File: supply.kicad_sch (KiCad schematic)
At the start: 66 parts, among them U5 PAC1934_QFN

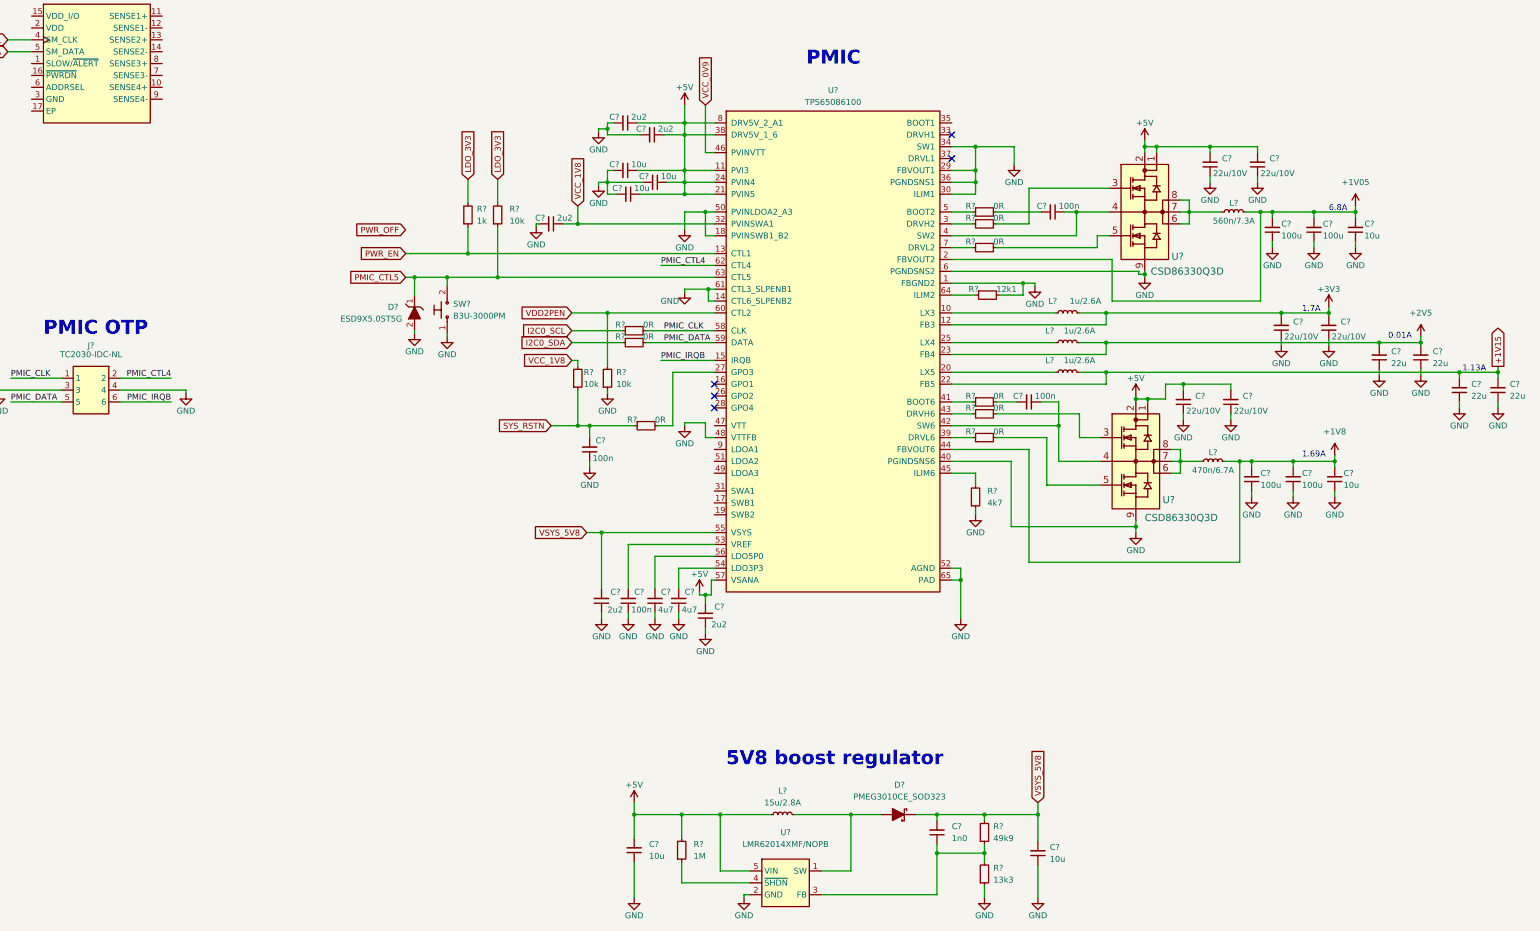
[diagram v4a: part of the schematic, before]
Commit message: [#52577] Change PMIC's inductors
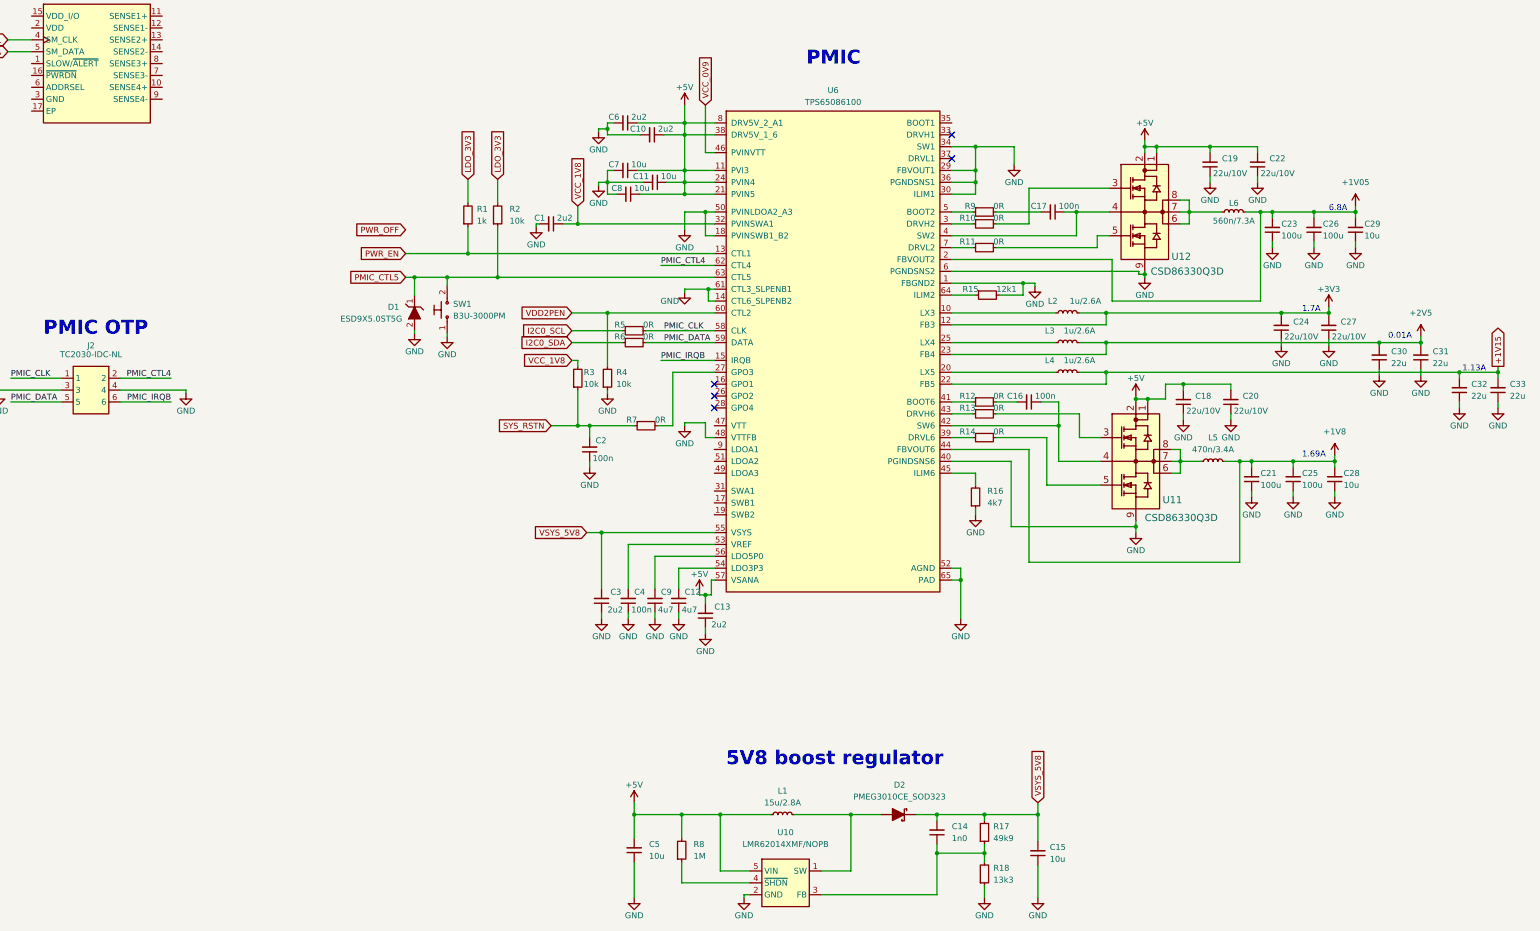
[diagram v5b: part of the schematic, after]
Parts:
- removed L?: L_470n_6.7A_Vishay-IHLP-1212AE-11, antmicro-footprints:L_Vishay-IHLP-1212AE, symbol antmicroFixedInductors:L_470n_6.7A_Vishay-IHLP-1212AE-11
- added L5: L_470n_3.4A_WE-MAIA-2512, antmicro-footprints:L_WE-MAIA-2512, symbol antmicroFixedInductors:L_470n_3.4A_WE-MAIA-2512
- gave numbers to parts that had none: 64
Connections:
- net +1V8: now also L5.2
- net at U11.6 (VSW), U11.7 (VSW), U11.8 (VSW): now also L5.1

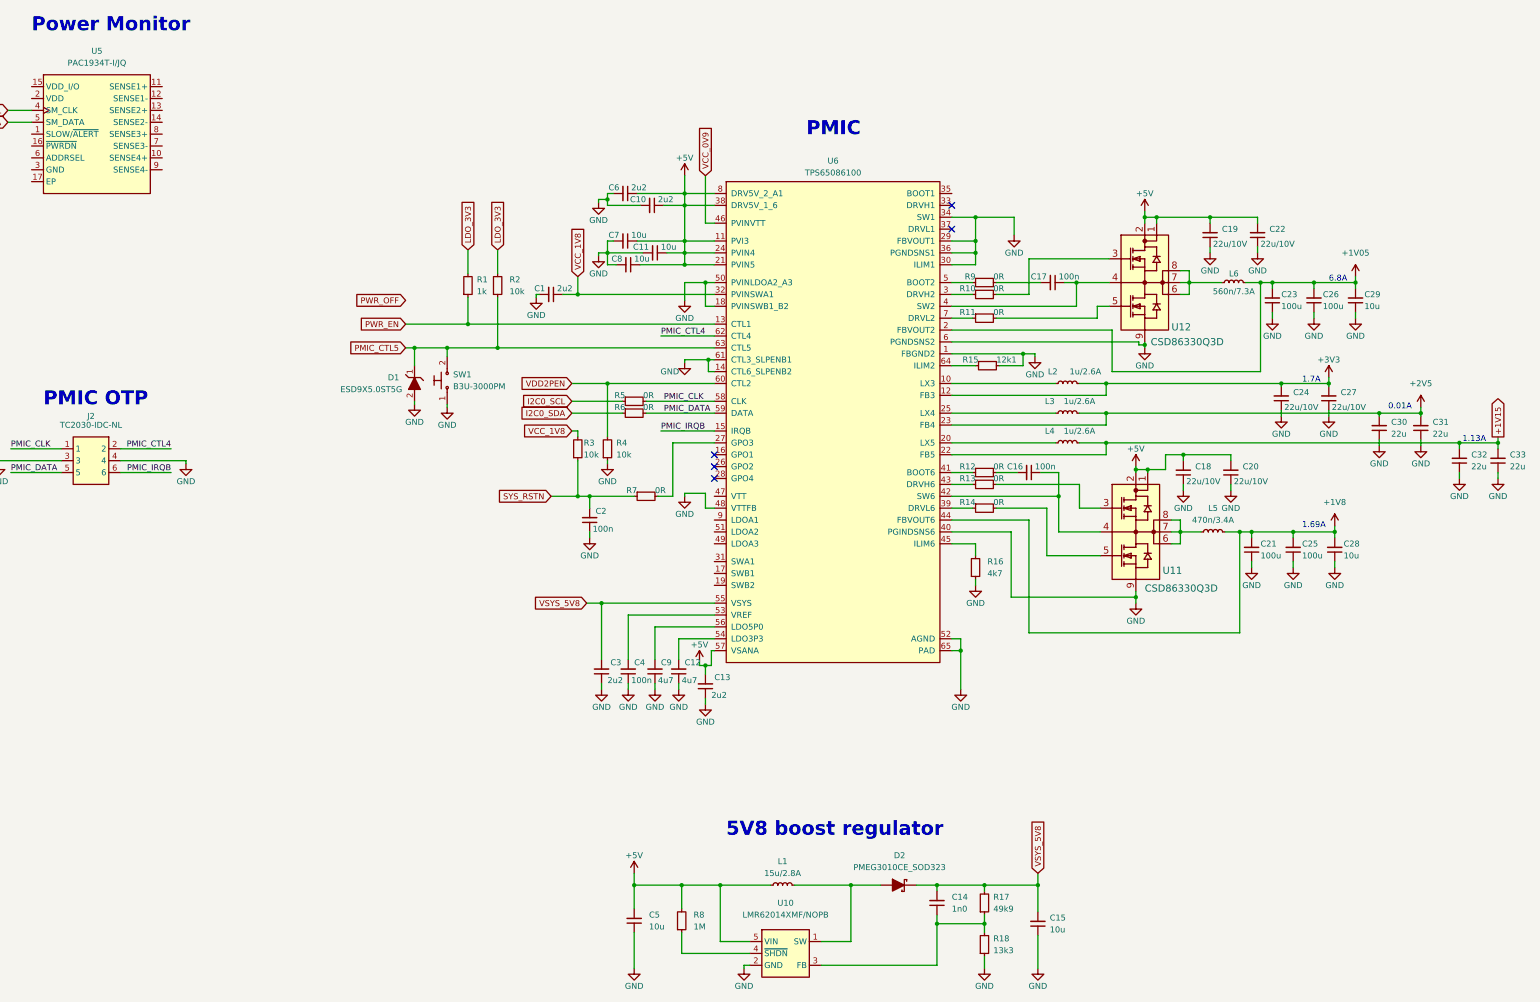
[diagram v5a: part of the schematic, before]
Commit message: [#52577] Clear annotations
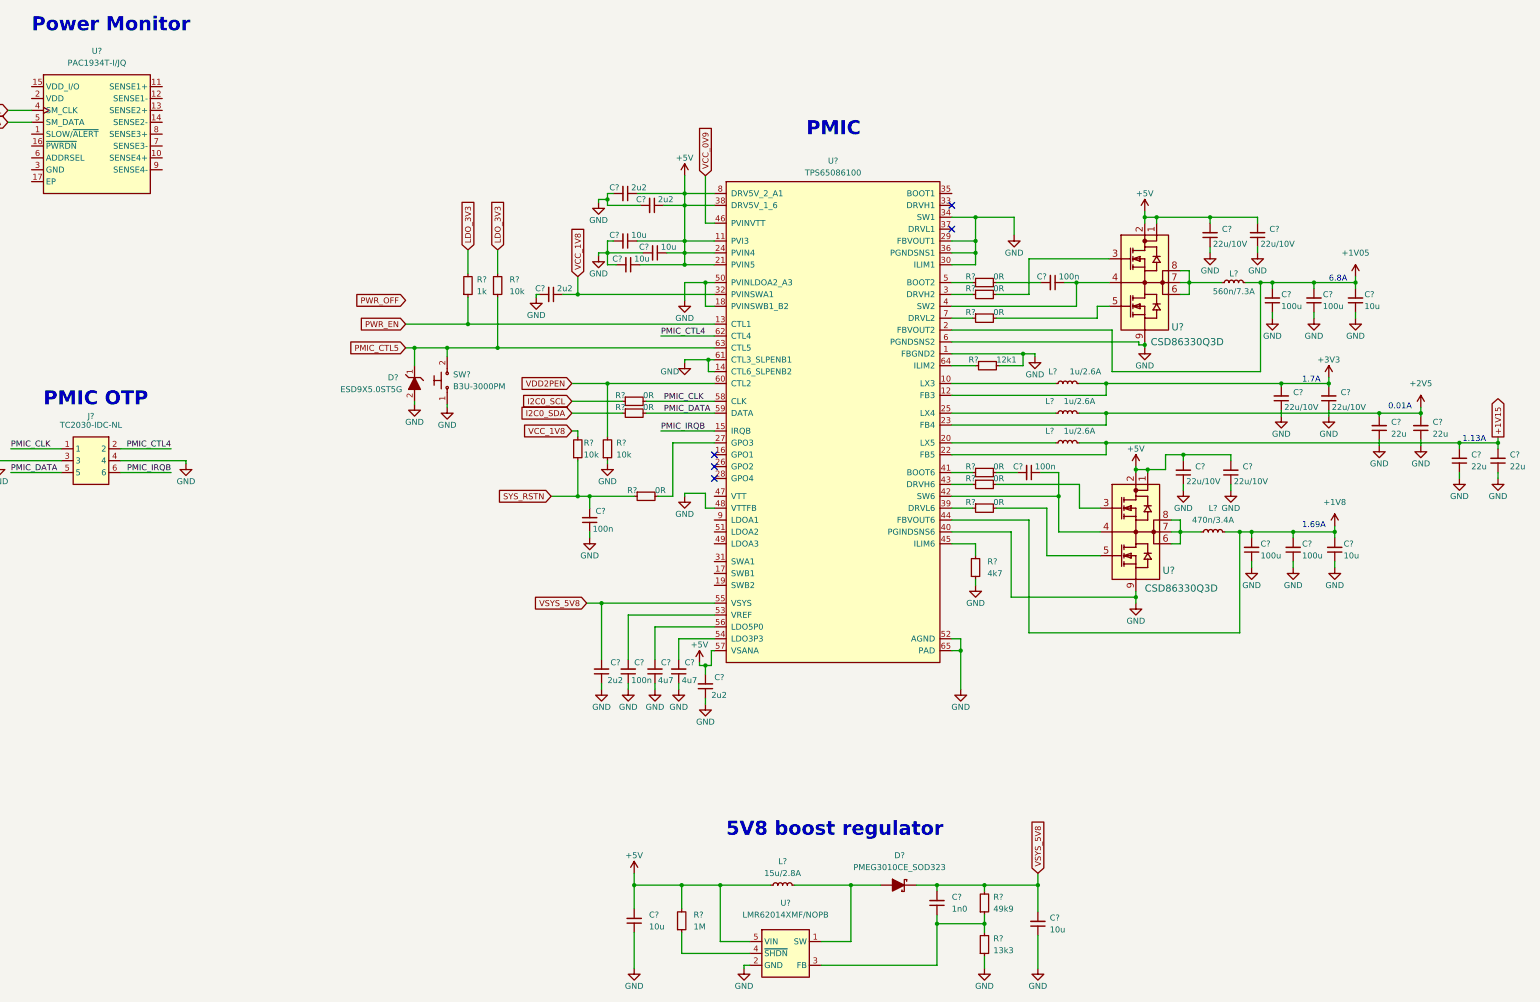
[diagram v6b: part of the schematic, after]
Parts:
- renumbered C14 to C?, C28 to C?, C31 to C?, C8 to C?, C29 to C?, C15 to C?, C13 to C?, C20 to C?, C4 to C?, C24 to C?, C5 to C?, C23 to C?, C18 to C?, C2 to C?, C21 to C?, C12 to C?, C3 to C?, C25 to C?, C30 to C?, C7 to C?, C27 to C?, C19 to C?, C9 to C?, C22 to C?, C10 to C?, C26 to C?, C6 to C?, C1 to C?, C33 to C?, C11 to C?, C32 to C?, C17 to C?, C16 to C?, D2 to D?, D1 to D?, J2 to J?, L6 to L?, L3 to L?, L1 to L?, L5 to L?, L4 to L?, L2 to L?, R9 to R?, R13 to R?, R10 to R?, R2 to R?, R7 to R?, R5 to R?, R15 to R?, R3 to R?, R4 to R?, R6 to R?, R17 to R?, R18 to R?, R14 to R?, R1 to R?, R12 to R?, R16 to R?, R11 to R?, R8 to R?, SW1 to SW?, U6 to U?, U12 to U?, U10 to U?, U5 to U?, U11 to U?
